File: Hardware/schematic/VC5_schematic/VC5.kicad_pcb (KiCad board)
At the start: 2 copper layers, 230 x 70 mm, 71 parts, among them J2 Debug_output, Q1 BC337, U1 1.3in SH1106 OLED, U2 1.3in SH1106 OLED, U3 1.3in SH1106 OLED, U4 1.3in SH1106 OLED, U5 1.3in SH1106 OLED, U6 MCP23017

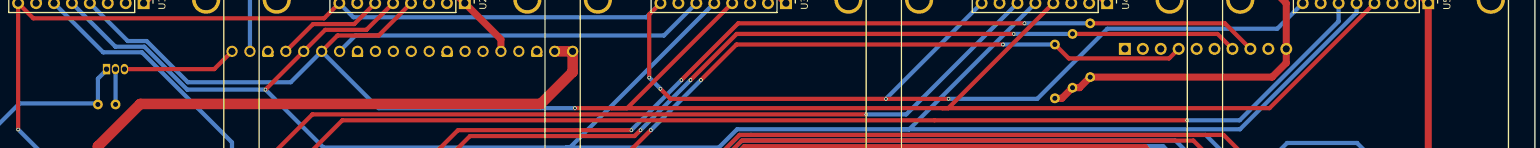
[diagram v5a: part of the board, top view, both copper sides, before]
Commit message: fixed missing interrupt line
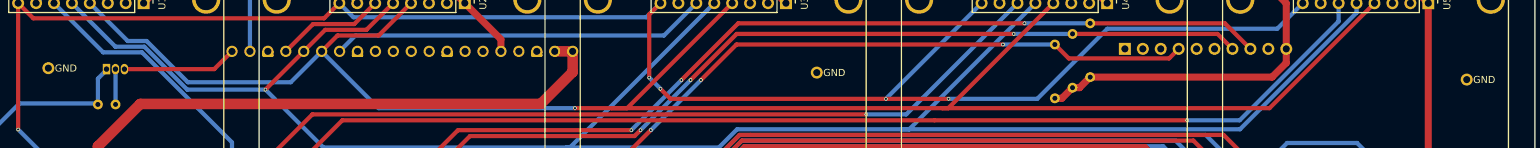
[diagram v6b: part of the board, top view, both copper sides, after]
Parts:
- added ?: , , F.Cu at (63.5, 74.3)
- added ?: , , F.Cu at (172.4, 74.9)
- added ?: , , F.Cu at (264.5, 75.9)
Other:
- board text added: "GND"
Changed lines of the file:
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@@
 		(embedded_fonts no)
 	)
+	(footprint ""
+		(layer "F.Cu")
+		(at 172.4 74.94)
+		(property "Reference" ""
+			(at 0 0 0)
+			(layer "F.SilkS")
+			(effects
+				(font
+					(size 1.27 1.27)
+					(thickness 0.15)
+				)
+			)
+		)
+		(property "Value" ""
+			(at 0 0 0)
+			(layer "F.Fab")
+			(effects
+				(font
+					(size 1.27 1.27)
+					(thickness 0.15)
+				)
+			)
+		)
+		(property "Datasheet" ""
+			(at 0 0 0)
+			(layer "F.Fab")
+			(hide yes)
+			(effects
+				(font
+					(size 1.27 1.27)
+					(thickness 0.15)
+				)
+			)
+		)
+		(property "Description" ""
+			(at 0 0 0)
+			(layer "F.Fab")
+			(hide yes)
+			(effects
+				(font
+					(size 1.27 1.27)
+					(thickness 0.15)
+				)
+			)
+		)
+		(pad "2" thru_hole oval
+			(at 0 0 270)
+			(size 1.7 1.7)
+			(drill 1)
+			(layers "*.Cu" "*.Mask")
+			(remove_unused_layers no)
+			(net 1 "GND")
+			(pinfunction "GND")
+			(pintype "power_in")
+		)
+		(embedded_fonts no)
+	)
 	(footprint "LED_THT:LED_D5.0mm-4_RGB_Wide_Pins"
 		(layer "F.Cu")
@@
 	(footprint ""
 		(layer "F.Cu")
+		(at 264.48 75.93)
+		(property "Reference" ""
+			(at 0 0 0)
+			(layer "F.SilkS")
+			(effects
+				(font
+					(size 1.27 1.27)
+					(thickness 0.15)
+				)
+			)
+		)
+		(property "Value" ""
+			(at 0 0 0)
+			(layer "F.Fab")
+			(effects
+				(font
+					(size 1.27 1.27)
+					(thickness 0.15)
+				)
+			)
+		)
+		(property "Datasheet" ""
+			(at 0 0 0)
+			(layer "F.Fab")
+			(hide yes)
+			(effects
+				(font
+					(size 1.27 1.27)
+					(thickness 0.15)
+				)
+			)
+		)
+		(property "Description" ""
+			(at 0 0 0)
+			(layer "F.Fab")
+			(hide yes)
+			(effects
+				(font
+					(size 1.27 1.27)
+					(thickness 0.15)
+				)
+			)
+		)
+		(pad "2" thru_hole oval
+			(at 0 0 270)
+			(size 1.7 1.7)
+			(drill 1)
+			(layers "*.Cu" "*.Mask")
+			(remove_unused_layers no)
+			(net 1 "GND")
+			(pinfunction "GND")
+			(pintype "power_in")
+		)
+		(embedded_fonts no)
+	)
+	(footprint ""
+		(layer "F.Cu")
 		(at 88.01 115.21)
 		(property "Reference" ""
@@
 		(embedded_fonts no)
 	)
+	(footprint ""
+		(layer "F.Cu")
+		(at 63.53 74.31)
+		(property "Reference" ""
+			(at 0 0 0)
+			(layer "F.SilkS")
+			(effects
+				(font
+					(size 1.27 1.27)
+					(thickness 0.15)
+				)
+			)
+		)
+		(property "Value" ""
+			(at 0 0 0)
+			(layer "F.Fab")
+			(effects
+				(font
+					(size 1.27 1.27)
+					(thickness 0.15)
+				)
+			)
+		)
+		(property "Datasheet" ""
+			(at 0 0 0)
+			(layer "F.Fab")
+			(hide yes)
+			(effects
+				(font
+					(size 1.27 1.27)
+					(thickness 0.15)
+				)
+			)
+		)
+		(property "Description" ""
+			(at 0 0 0)
+			(layer "F.Fab")
+			(hide yes)
+			(effects
+				(font
+					(size 1.27 1.27)
+					(thickness 0.15)
+				)
+			)
+		)
+		(pad "2" thru_hole oval
+			(at 0 0 270)
+			(size 1.7 1.7)
+			(drill 1)
+			(layers "*.Cu" "*.Mask")
+			(remove_unused_layers no)
+			(net 1 "GND")
+			(pinfunction "GND")
+			(pintype "power_in")
+		)
+		(embedded_fonts no)
+	)
 	(footprint "VC5_footprint_library:PinHeader_1x08_P2.54mm_Vertical_Display"
 		(layer "F.Cu")
@@
 		)
 	)
+	(gr_text "GND"
+		(at 66.01 74.33 0)
+		(layer "F.SilkS")
+		(effects
+			(font
+				(size 1 1)
+				(thickness 0.15)
+			)
+		)
+	)
+	(gr_text "GND"
+		(at 174.88 74.96 0)
+		(layer "F.SilkS")
+		(effects
+			(font
+				(size 1 1)
+				(thickness 0.15)
+			)
+		)
+	)
+	(gr_text "GND"
+		(at 266.96 75.95 0)
+		(layer "F.SilkS")
+		(effects
+			(font
+				(size 1 1)
+				(thickness 0.15)
+			)
+		)
+	)
+	(gr_text "GND"
+		(at 174.89 74.95 0)
+		(layer "B.SilkS")
+		(effects
+			(font
+				(size 1 1)
+				(thickness 0.15)
+			)
+			(justify mirror)
+		)
+	)
+	(gr_text "GND"
+		(at 266.94 75.94 0)
+		(layer "B.SilkS")
+		(effects
+			(font
+				(size 1 1)
+				(thickness 0.15)
+			)
+			(justify mirror)
+		)
+	)
+	(gr_text "GND"
+		(at 66.03 74.32 0)
+		(layer "B.SilkS")
+		(effects
+			(font
+				(size 1 1)
+				(thickness 0.15)
+			)
+			(justify mirror)
+		)
+	)

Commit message: final version of the PCB
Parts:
- added ?: , , F.Cu at (228.4, 63.4)
- added ?: , , F.Cu at (180.9, 89.6)
- added ?: , , F.Cu at (84.0, 69.8)
- added ?: , , F.Cu at (143.0, 68.8)
- added ?: , , F.Cu at (228.4, 77.5)
- added ?: , , F.Cu at (126.8, 64.5)
- added ?: , , F.Cu at (157.2, 83.5)
- added ?: , , F.Cu at (243.1, 76.0)
- added ?: , , F.Cu at (164.8, 95.9)
- added R26: 10k, Resistor_THT:R_Axial_DIN0204_L3.6mm_D1.6mm_P7.62mm_Horizontal, B.Cu at (198.2, 90.2)
- moved C10 0.10 mm to (141.7, 104.1)
- moved C12 0.10 mm to (187.3, 104.1)
- moved C14 0.10 mm to (232.7, 104.1)
- moved C6 0.10 mm to (50.7, 104.1)
- moved C8 0.10 mm to (96.2, 104.1)
- moved R11 0.10 mm to (101.6, 104.1)
- moved R15 0.10 mm to (147.1, 104.1)
- moved R19 0.10 mm to (192.8, 104.1)
- moved R23 0.10 mm to (238.1, 104.1)
- moved R4 0.10 mm to (56.1, 104.1)
- moved R12 0.10 mm to (99.1, 111.7)
- moved R16 0.10 mm to (144.6, 111.7)
- moved R20 0.10 mm to (190.2, 111.7)
- moved R24 0.10 mm to (235.6, 111.7)
- moved R5 0.10 mm to (53.6, 111.7)
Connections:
- A1 pad 5: unconnected-(A1-GPIO3-Pad5) -> /rotaries/MCP_INT
- U6 pad 16: unconnected-(U6-INTA-Pad16) -> /rotaries/MCP_INT
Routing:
- net /rotaries/MCP_INT: track 0.00 -> 242.2 mm, vias 0 -> 1
- net +3.3V: track 630.1 -> 634.2 mm
- net /displays/D/C: track 207.9 -> 211.2 mm
- net /displays/DIN: track 258.6 -> 261.4 mm
- net /displays/DISP_RESET: track 293.6 -> 291.0 mm
- net Net-(U6-GPB4): track 191.7 -> 191.8 mm, vias 0 -> 1
